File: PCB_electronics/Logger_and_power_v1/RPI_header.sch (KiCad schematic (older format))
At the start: 1 part

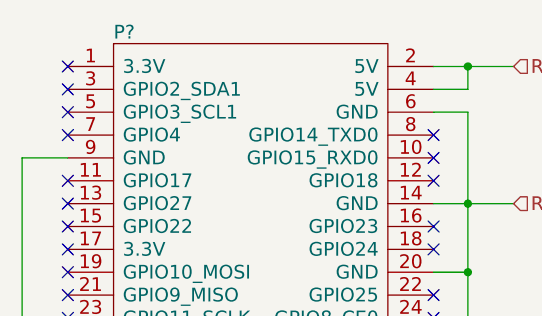
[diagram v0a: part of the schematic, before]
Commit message: corrected shape of the board; added missing wire
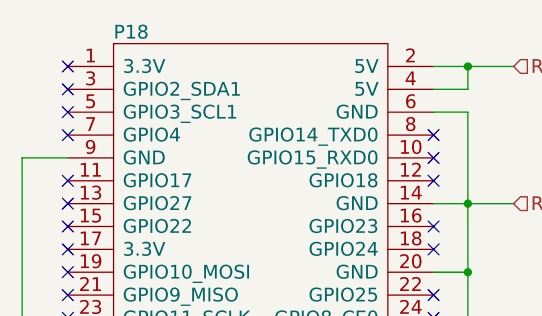
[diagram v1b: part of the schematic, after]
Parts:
- P18: renamed from P?; footprint (none) -> Pin_Headers:Pin_Header_Straight_2x20
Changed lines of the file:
@@
 $EndDescr
 $Comp
-L RASPBERRYPI2 P?
+L RASPBERRYPI2 P18
 U 1 1 5B0BE3C0
 P 3200 3000
-F 0 "P?" H 2600 4150 60  0000 L CNN
+F 0 "P18" H 2600 4150 60  0000 L CNN
 F 1 "RASPBERRYPI2" H 2600 1950 60  0000 L CNN
-F 2 "" H 3000 2200 60  0000 C CNN
+F 2 "Pin_Headers:Pin_Header_Straight_2x20" H 3000 2200 60  0001 C CNN
 F 3 "" H 3000 2200 60  0000 C CNN
 	1    3200 3000
